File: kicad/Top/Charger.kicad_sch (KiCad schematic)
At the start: 0 parts

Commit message: Removed all charger chip schematics
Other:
- removed sheet Charger_Circuit
- removed sheet Charger_Msc
- removed sheet HostInterface
- removed sheet InputSourceSelection
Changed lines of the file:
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@@
 (kicad_sch (version 20211123) (generator eeschema)
   (paper "A")
-  (wire (pts (xy 81.28 93.98) (xy 99.06 93.98))
-    (stroke (width 0.254) (type default) (color 0 0 0 0))
-  )
-  (wire (pts (xy 81.28 96.52) (xy 99.06 96.52))
-    (stroke (width 0.254) (type default) (color 0 0 0 0))
-  )
-  (wire (pts (xy 81.28 88.9) (xy 99.06 88.9))
-    (stroke (width 0.254) (type default) (color 0 0 0 0))
-  )
-  (wire (pts (xy 81.28 86.36) (xy 99.06 86.36))
-    (stroke (width 0.254) (type default) (color 0 0 0 0))
-  )
-  (wire (pts (xy 86.36 177.8) (xy 101.6 177.8))
-    (stroke (width 0.254) (type default) (color 0 0 0 0))
-  )
-  (wire (pts (xy 81.28 111.76) (xy 104.14 111.76))
-    (stroke (width 0.254) (type default) (color 0 0 0 0))
-  )
-  (wire (pts (xy 101.6 177.8) (xy 101.6 114.3))
-    (stroke (width 0.254) (type default) (color 0 0 0 0))
-  )
-  (wire (pts (xy 81.28 99.06) (xy 99.06 99.06))
-    (stroke (width 0.254) (type default) (color 0 0 0 0))
-  )
-  (wire (pts (xy 81.28 104.14) (xy 99.06 104.14))
-    (stroke (width 0.254) (type default) (color 0 0 0 0))
-  )
-  (wire (pts (xy 81.28 101.6) (xy 99.06 101.6))
-    (stroke (width 0.254) (type default) (color 0 0 0 0))
-  )
-  (wire (pts (xy 86.36 76.2) (xy 81.28 76.2))
-    (stroke (width 0.254) (type default) (color 0 0 0 0))
-  )
-  (wire (pts (xy 104.14 180.34) (xy 86.36 180.34))
-    (stroke (width 0.254) (type default) (color 0 0 0 0))
-  )
-  (wire (pts (xy 86.36 78.74) (xy 81.28 78.74))
-    (stroke (width 0.254) (type default) (color 0 0 0 0))
-  )
-  (wire (pts (xy 101.6 114.3) (xy 81.28 114.3))
-    (stroke (width 0.254) (type default) (color 0 0 0 0))
-  )
-  (wire (pts (xy 81.28 106.68) (xy 99.06 106.68))
-    (stroke (width 0.254) (type default) (color 0 0 0 0))
-  )
-  (wire (pts (xy 104.14 111.76) (xy 104.14 180.34))
-    (stroke (width 0.254) (type default) (color 0 0 0 0))
-  )
-  (label "SDA" (at 91.44 180.34 0)
-    (effects (font (size 1.27 1.27)) (justify left bottom))
-  )
-  (label "SCL" (at 91.44 177.8 0)
-    (effects (font (size 1.27 1.27)) (justify left bottom))
-  )
-  (global_label "D+" (shape input) (at 86.36 76.2 0) (fields_autoplaced)
-    (effects (font (size 1.27 1.27)) (justify left))
-    (property "Intersheet References" "${INTERSHEET_REFS}" (id 0) (at 0 0 0)
-      (effects (font (size 1.27 1.27)) hide)
-    )
-  )
-  (global_label "D-" (shape input) (at 86.36 78.74 0) (fields_autoplaced)
-    (effects (font (size 1.27 1.27)) (justify left))
-    (property "Intersheet References" "${INTERSHEET_REFS}" (id 0) (at 0 0 0)
-      (effects (font (size 1.27 1.27)) hide)
-    )
-  )
-  (sheet (at 43.18 167.64) (size 43.18 15.24) (fields_autoplaced)
-    (stroke (width 0) (type solid) (color 128 0 0 1))
-    (fill (color 128 255 128 1.0000))
-    (property "Sheet name" "HostInterface" (id 0) (at 43.18 166.9284 0)
-      (effects (font (size 1.27 1.27)) (justify left bottom))
-    )
-    (property "Sheet file" "HostInterface.kicad_sch" (id 1) (at 43.18 183.4646 0)
-      (effects (font (size 1.27 1.27)) (justify left top))
-    )
-    (pin "SCL" output (at 86.36 177.8 0)
-      (effects (font (size 1.27 1.27)) (justify right))
-    )
-    (pin "SDA" bidirectional (at 86.36 180.34 0)
-      (effects (font (size 1.27 1.27)) (justify right))
-    )
-    (pin "Power_Charger" passive (at 86.36 170.18 0)
-      (effects (font (size 1.27 1.27)) (justify right))
-    )
-    (pin "Power_External" passive (at 43.18 172.72 180)
-      (effects (font (size 1.27 1.27)) (justify left))
-    )
-  )
-  (sheet (at 43.18 73.66) (size 38.1 50.8) (fields_autoplaced)
-    (stroke (width 0) (type solid) (color 128 0 0 1))
-    (fill (color 128 255 128 1.0000))
-    (property "Sheet name" "Charger_Circuit" (id 0) (at 43.18 72.9484 0)
-      (effects (font (size 1.27 1.27)) (justify left bottom))
-    )
-    (property "Sheet file" "Charger_Circuit.kicad_sch" (id 1) (at 43.18 125.0446 0)
-      (effects (font (size 1.27 1.27)) (justify left top))
-    )
-    (pin "D+" input (at 81.28 76.2 0)
-      (effects (font (size 1.27 1.27)) (justify right))
-    )
-    (pin "D-" input (at 81.28 78.74 0)
-      (effects (font (size 1.27 1.27)) (justify right))
-    )
-    (pin "ILIM_HIZ" input (at 81.28 93.98 0)
-      (effects (font (size 1.27 1.27)) (justify right))
-    )
-    (pin "PROG" input (at 81.28 88.9 0)
-      (effects (font (size 1.27 1.27)) (justify right))
-    )
-    (pin "/QON" input (at 81.28 106.68 0)
-      (effects (font (size 1.27 1.27)) (justify right))
-    )
-    (pin "/PG" output (at 81.28 101.6 0)
-      (effects (font (size 1.27 1.27)) (justify right))
-    )
-    (pin "/INT" passive (at 81.28 96.52 0)
-      (effects (font (size 1.27 1.27)) (justify right))
-    )
-    (pin "STAT" output (at 81.28 104.14 0)
-      (effects (font (size 1.27 1.27)) (justify right))
-    )
-    (pin "/CE" input (at 81.28 99.06 0)
-      (effects (font (size 1.27 1.27)) (justify right))
-    )
-    (pin "SCL" input (at 81.28 114.3 0)
-      (effects (font (size 1.27 1.27)) (justify right))
-    )
-    (pin "SDA" bidirectional (at 81.28 111.76 0)
-      (effects (font (size 1.27 1.27)) (justify right))
-    )
-    (pin "TS" input (at 81.28 86.36 0)
-      (effects (font (size 1.27 1.27)) (justify right))
-    )
-    (pin "Power_External" passive (at 43.18 78.74 180)
-      (effects (font (size 1.27 1.27)) (justify left))
-    )
-    (pin "Power_Charger" passive (at 81.28 119.38 0)
-      (effects (font (size 1.27 1.27)) (justify right))
-    )
-  )
-  (sheet (at 99.06 81.28) (size 38.1 27.94) (fields_autoplaced)
-    (stroke (width 0) (type solid) (color 128 0 0 1))
-    (fill (color 128 255 128 1.0000))
-    (property "Sheet name" "Charger_Msc" (id 0) (at 99.06 80.5684 0)
-      (effects (font (size 1.27 1.27)) (justify left bottom))
-    )
-    (property "Sheet file" "Charger_Msc.kicad_sch" (id 1) (at 99.06 109.8046 0)
-      (effects (font (size 1.27 1.27)) (justify left top))
-    )
-    (pin "/INT" passive (at 99.06 96.52 180)
-      (effects (font (size 1.27 1.27)) (justify left))
-    )
-    (pin "TS" output (at 99.06 86.36 180)
-      (effects (font (size 1.27 1.27)) (justify left))
-    )
-    (pin "/CE" output (at 99.06 99.06 180)
-      (effects (font (size 1.27 1.27)) (justify left))
-    )
-    (pin "ILIM_HIZ" output (at 99.06 93.98 180)
-      (effects (font (size 1.27 1.27)) (justify left))
-    )
-    (pin "/PG" input (at 99.06 101.6 180)
-      (effects (font (size 1.27 1.27)) (justify left))
-    )
-    (pin "STAT" input (at 99.06 104.14 180)
-      (effects (font (size 1.27 1.27)) (justify left))
-    )
-    (pin "/QON" output (at 99.06 106.68 180)
-      (effects (font (size 1.27 1.27)) (justify left))
-    )
-    (pin "PROG" output (at 99.06 88.9 180)
-      (effects (font (size 1.27 1.27)) (justify left))
-    )
-    (pin "Power_Charger" passive (at 137.16 106.68 0)
-      (effects (font (size 1.27 1.27)) (justify right))
-    )
-    (pin "Power_External" passive (at 137.16 83.82 0)
-      (effects (font (size 1.27 1.27)) (justify right))
-    )
-  )
-  (sheet (at 43.18 132.08) (size 43.18 10.16) (fields_autoplaced)
-    (stroke (width 0) (type solid) (color 128 0 0 1))
-    (fill (color 128 255 128 1.0000))
-    (property "Sheet name" "InputSourceSelection" (id 0) (at 43.18 131.3684 0)
-      (effects (font (size 1.27 1.27)) (justify left bottom))
-    )
-    (property "Sheet file" "InputSourceSelection.kicad_sch" (id 1) (at 43.18 142.8246 0)
-      (effects (font (size 1.27 1.27)) (justify left top))
-    )
-    (pin "Power_External" passive (at 43.18 137.16 180)
-      (effects (font (size 1.27 1.27)) (justify left))
-    )
-    (pin "Power_Charger" passive (at 86.36 137.16 0)
-      (effects (font (size 1.27 1.27)) (justify right))
-    )
-  )
   (sheet_instances
     (path "/" (page "4"))

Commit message: Added initial battery charger schematic based on typical application circuit and pin descriptions
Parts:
- added BT?: Battery_Cell, symbol Device:Battery_Cell
- added C? (x5): 10uF, symbol Device:C
- added C? (x2): 1uF, symbol Device:C
- added C? (x2): 0.1uF, symbol Device:C
- added C? (x3): DNP, symbol Device:C
- added C?: 100nF, symbol Device:C
- added C? (x2): 22uF, symbol Device:C
- added C?: 10nF, symbol Device:C
- added D?: LED, symbol Device:LED
- added D?: D_Schottky, symbol Device:D_Schottky
- added L?: 0.47uH, symbol pspice:INDUCTOR
- added R? (x2): 1.5k, symbol Device:R
- added R? (x2): 10k, symbol Device:R
- added R?: 100k, symbol Device:R
- added TH?: 10k, symbol Device:Thermistor
- added U?: MAX77976EFD+, Ultra_Librarian:MAX77976, symbol ultralibrarian:MAX77976EFD+
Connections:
- new net: BT?.1 (+), C?.1, U?.5 (BATSP), U?.6 (BATT), U?.7 (BATT), U?.8 (BATT)
- new net: C?.1, U?.3 (VDD)
- new net: C?.2, L?.1, U?.17 (LX), U?.18 (LX), U?.19 (LX)
- new net: C?.1, R?.1, TH?.1, U?.2 (THM)
- new net: C?.1, U?.20 (BST)
- new net: C?.1, C?.1, D?.1 (K), U?.21 (BYP)
- new net: D?.1 (K), U?.29 (STAT)
- new net: R?.1, U?.30 (QBEXT)
- new net AGND: BT?.2 (-), C?.2, C?.2, C?.2, C?.2, C?.2, C?.2, C?.2, C?.2, C?.2, C?.2, C?.2, C?.2, C?.2, C?.2, C?.2, TH?.2, U?.13 (DGND), U?.14 (PGND), U?.15 (PGND), U?.16 (PGND), U?.28 (AGND), U?.4 (BATSN)
- new net DISQBAT: U?.1 (DISQBAT)
- new net EXTSM: U?.26 (EXTSM)
- new net IRQB: R?.2, U?.32 (IRQB)
- new net PVDD: C?.1, C?.1, R?.2, U?.12 (PVDD)
- new net SCL: R?.2, U?.24 (SCL)
- new net SDA: R?.2, U?.25 (SDA)
- new net SUSPND: U?.31 (SUSPND)
- new net SYS: C?.1, C?.1, C?.1, C?.1, C?.1, D?.2 (A), L?.2, U?.10 (SYS), U?.11 (SYS), U?.9 (SYS)
- new net VIO: C?.1, R?.1, R?.1, R?.1, R?.2, U?.27 (VIO)
- new net V_IN: C?.1, C?.1, D?.2 (A), U?.22 (CHGIN), U?.23 (CHGIN)
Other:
- note added: "Connect as close as possible to batt"

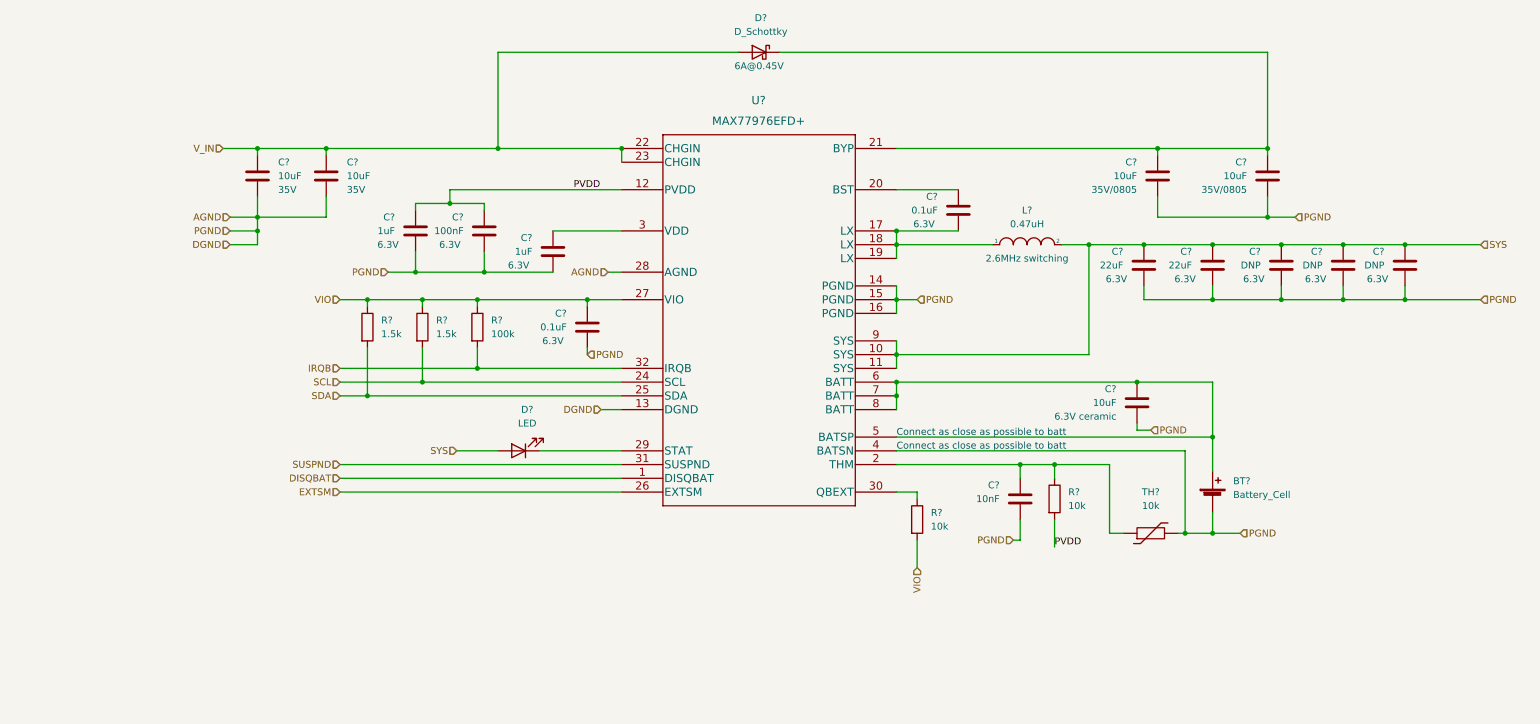
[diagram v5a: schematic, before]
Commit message: Updated battery charger based on eval board schematic
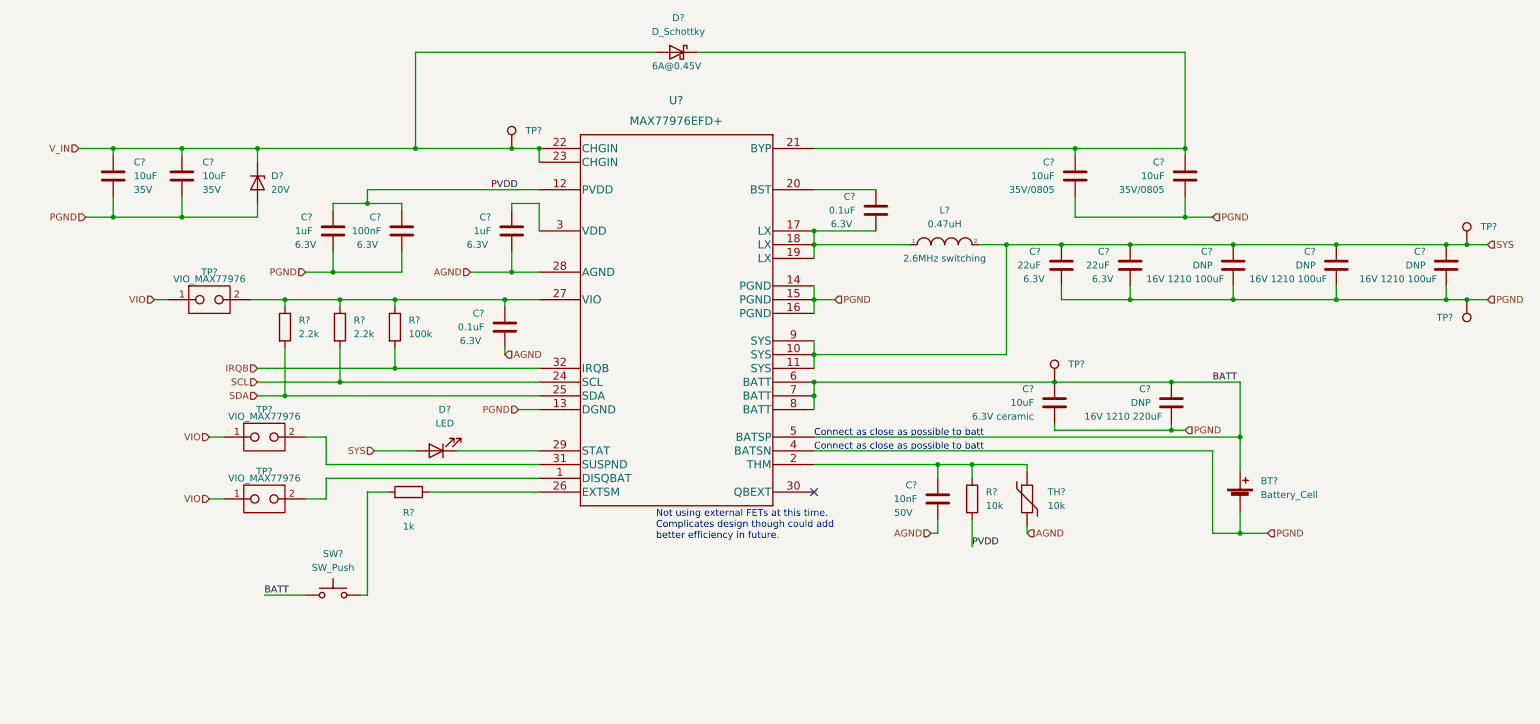
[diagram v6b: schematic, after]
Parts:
- removed C? (x2): DNP, symbol Device:C
- removed R?: 10k, symbol Device:R
- added C? (x3): DNP, symbol Device:C
- added D?: 20V, symbol Device:D_Zener
- added R?: 1k, symbol Device:R
- added SW?: SW_Push, symbol Switch:SW_Push
- added TP? (x3): VIO_MAX77976, custom_connectors:2.54mm_2pointCurrentTestPoint, symbol custom_connectors:TestPoint_CurrentShunt
- added TP? (x4): TestPoint, symbol Connector:TestPoint
- R? (x2): value 1.5k -> 2.2k
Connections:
- net AGND: no longer BT?.2 (-), C?.2, C?.2, C?.2, C?.2, C?.2, C?.2, C?.2, C?.2, C?.2, C?.2, U?.13 (DGND), U?.14 (PGND), U?.15 (PGND), U?.16 (PGND), U?.4 (BATSN)
- net SYS: now also C?.1, C?.1, TP?.1
- net VIO: now also TP?.1, TP?.1, TP?.1; no longer C?.1, R?.1, R?.1, R?.1, U?.27 (VIO)
- net V_IN: now also D?.1 (K), TP?.1
- net BATT: now reaches BT?.1 (+), C?.1, U?.5 (BATSP), U?.6 (BATT), U?.7 (BATT), U?.8 (BATT)
- net BATT: now also C?.1, SW?.1, TP?.1
- net DISQBAT: no longer names the net of U?.1 (DISQBAT)
- net DISQBAT: now also TP?.2
- net EXTSM: no longer names the net of U?.26 (EXTSM)
- net EXTSM: now also R?.1
- net SUSPND: no longer names the net of U?.31 (SUSPND)
- net SUSPND: now also TP?.2
- new net: C?.1, R?.1, R?.1, R?.1, TP?.2, U?.27 (VIO)
- new net: R?.2, SW?.2
- new net PGND: BT?.2 (-), C?.2, C?.2, C?.2, C?.2, C?.2, C?.2, C?.2, C?.2, C?.2, C?.2, C?.2, C?.2, C?.2, D?.2 (A), TP?.1, U?.13 (DGND), U?.14 (PGND), U?.15 (PGND), U?.16 (PGND), U?.4 (BATSN)
- no-connect marks 0 -> 1
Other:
- note added: "Not using external FETs at this time. Complicates design though could add better efficiency in future."
- moved on the sheet: BT?, C?, D?, L?, R?, TH?, U?

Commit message: wip
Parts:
- TP?: Default Disconnected -> (none); Populated (none) -> No
- TP?: Default Connected -> (none); Populated (none) -> Yes
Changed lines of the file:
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@@
       (effects (font (size 1.27 1.27)) hide)
     )
-    (property "Default" "Disconnected" (id 13) (at 45.72 134.62 0)
+    (property "Populated" "No" (id 4) (at 45.72 134.62 0)
       (effects (font (size 1.27 1.27)) hide)
     )
@@
       (effects (font (size 1.27 1.27)) hide)
     )
-    (property "Default" "Connected" (id 13) (at 35.56 109.22 0)
-      (effects (font (size 1.27 1.27)) hide)
-    )
+    (property "Populated" "Yes" (id 4) (at 35.56 109.22 0)
+      (effects (font (size 1.27 1.27)) hide)
+    )
